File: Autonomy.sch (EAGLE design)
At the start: 5 parts, among them J1 APP_2POS_CONFIG12V_HORIZ, K1 PIN20X2, U1 OKI-78SR-5/1.5-W36HC

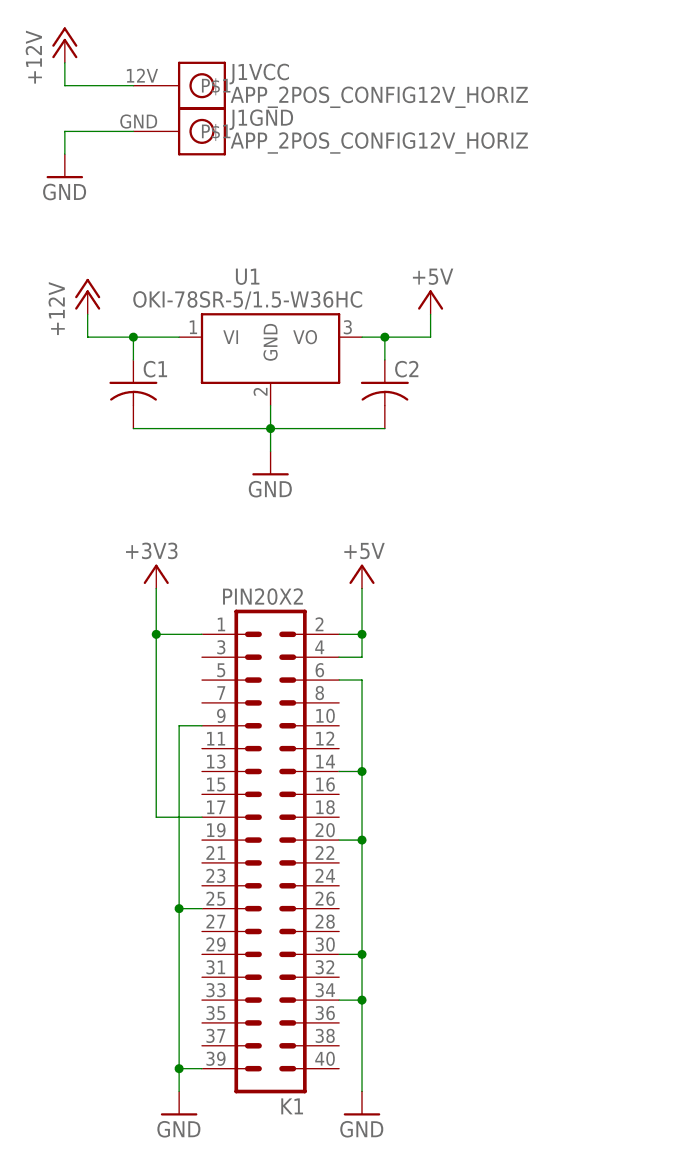
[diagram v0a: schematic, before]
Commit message: Cleaned up board, added power LED and board label
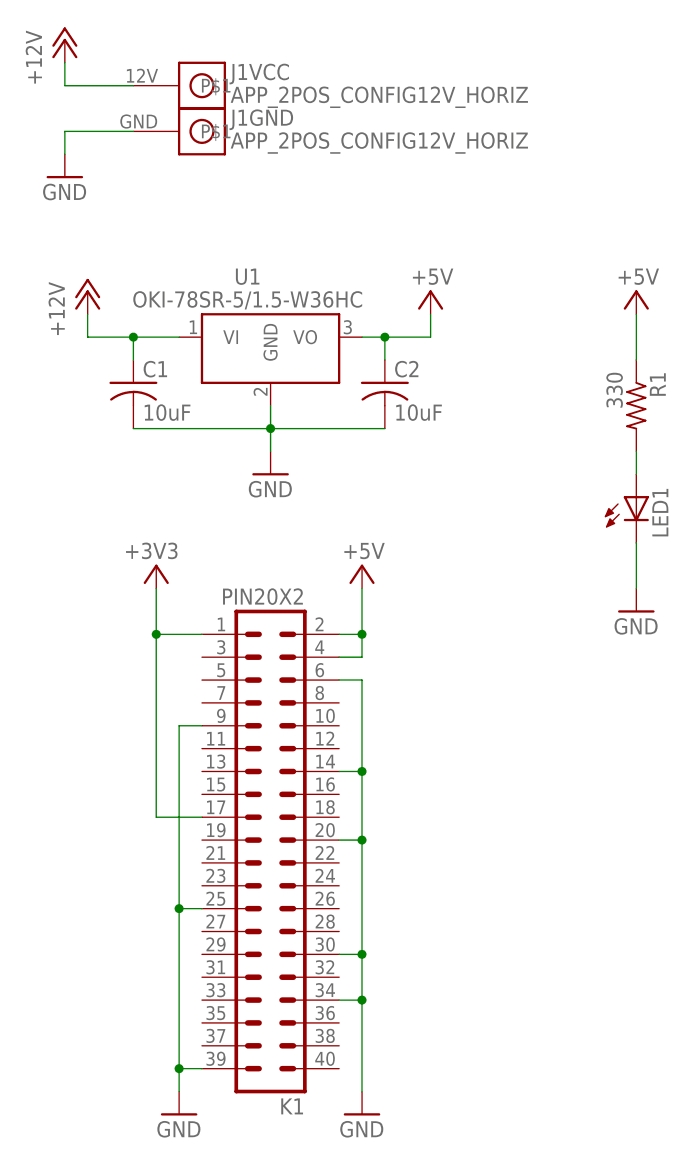
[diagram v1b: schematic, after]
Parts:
- added LED1: (no value), led:LEDCHIPLED_1206
- added R1: 330, rcl:R-US_R1206
- C1, C2: value (none) -> 10uF
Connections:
- new net N$1: LED1.A, R1.2
- net +5V: now also R1.1
- net GND: now also LED1.C
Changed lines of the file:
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@@
 <?xml version="1.0" encoding="utf-8"?>
 <!DOCTYPE eagle SYSTEM "eagle.dtd">
-<eagle version="7.4.0">
+<eagle version="7.5.0">
 <drawing>
 <settings>
@@
 <part name="GND2" library="supply1" deviceset="GND" device=""/>
 <part name="P+4" library="supply1" deviceset="+5V" device=""/>
-<part name="C1" library="rcl" deviceset="C-US" device="C1206"/>
-<part name="C2" library="rcl" deviceset="C-US" device="C1206"/>
+<part name="C1" library="rcl" deviceset="C-US" device="C1206" value="10uF"/>
+<part name="C2" library="rcl" deviceset="C-US" device="C1206" value="10uF"/>
+<part name="P+5" library="supply1" deviceset="+5V" device=""/>
+<part name="LED1" library="led" deviceset="LED" device="CHIPLED_1206"/>
+<part name="R1" library="rcl" deviceset="R-US_" device="R1206" value="330"/>
+<part name="GND4" library="supply1" deviceset="GND" device=""/>
 </parts>
 <sheets>
@@
 <instance part="C1" gate="G$1" x="30.48" y="22.86"/>
 <instance part="C2" gate="G$1" x="58.42" y="22.86"/>
+<instance part="P+5" gate="1" x="86.36" y="33.02" smashed="yes">
+<attribute name="VALUE" x="88.9" y="35.56" size="1.778" layer="96" rot="R180"/>
+</instance>
+<instance part="LED1" gate="G$1" x="86.36" y="10.16"/>
+<instance part="R1" gate="G$1" x="86.36" y="20.32" rot="R270"/>
+<instance part="GND4" gate="1" x="86.36" y="-2.54"/>
 </instances>
 <busses>
@@
 <wire x1="22.86" y1="50.8" x2="30.48" y2="50.8" width="0.1524" layer="91"/>
 </segment>
+<segment>
+<pinref part="GND4" gate="1" pin="GND"/>
+<pinref part="LED1" gate="G$1" pin="C"/>
+<wire x1="86.36" y1="0" x2="86.36" y2="5.08" width="0.1524" layer="91"/>
+</segment>
 </net>
 <net name="+3V3" class="0">
@@
 <junction x="58.42" y="27.94"/>
 </segment>
+<segment>
+<pinref part="P+5" gate="1" pin="+5V"/>
+<pinref part="R1" gate="G$1" pin="1"/>
+<wire x1="86.36" y1="25.4" x2="86.36" y2="30.48" width="0.1524" layer="91"/>
+</segment>
 </net>
 <net name="+12V" class="0">
@@
 </segment>
 </net>
+<net name="N$1" class="0">
+<segment>
+<pinref part="LED1" gate="G$1" pin="A"/>
+<pinref part="R1" gate="G$1" pin="2"/>
+<wire x1="86.36" y1="12.7" x2="86.36" y2="15.24" width="0.1524" layer="91"/>
+</segment>
+</net>

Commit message: Removed unnecessary 3v3 net and swapped header with eagle standard part
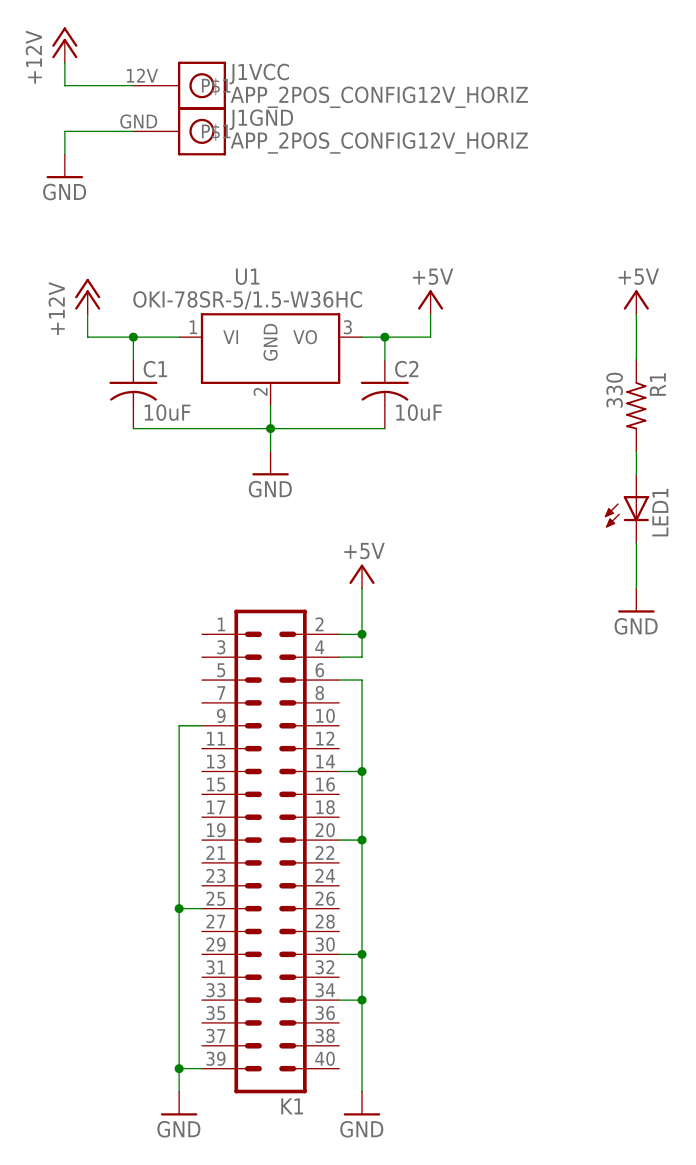
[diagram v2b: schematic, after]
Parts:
- K1: value PIN20X2 -> (none); device FLYFISH:PIN20X2 -> con-lstb:MA20-2
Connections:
- removed net +3V3: K1.1, K1.17
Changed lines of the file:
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@@
 </classes>
 <parts>
-<part name="K1" library="FLYFISH" deviceset="PIN20X2" device=""/>
+<part name="K1" library="con-lstb" deviceset="MA20-2" device=""/>
 <part name="GND10" library="supply1" deviceset="GND" device=""/>
-<part name="+3V1" library="supply1" deviceset="+3V3" device=""/>
 <part name="GND3" library="supply1" deviceset="GND" device=""/>
 <part name="P+1" library="supply1" deviceset="+5V" device=""/>
@@
 </plain>
 <instances>
-<instance part="K1" gate="G$1" x="45.72" y="-27.94" rot="R180"/>
+<instance part="K1" gate="G$1" x="45.72" y="-30.48" rot="R180"/>
 <instance part="GND10" gate="1" x="55.88" y="-58.42"/>
-<instance part="+3V1" gate="G$1" x="33.02" y="2.54" smashed="yes">
-<attribute name="VALUE" x="35.56" y="5.08" size="1.778" layer="96" rot="R180"/>
-</instance>
 <instance part="GND3" gate="1" x="35.56" y="-58.42"/>
 <instance part="P+1" gate="1" x="55.88" y="2.54" smashed="yes">
@@
 </segment>
 </net>
-<net name="+3V3" class="0">
-<segment>
-<pinref part="K1" gate="G$1" pin="1"/>
-<pinref part="+3V1" gate="G$1" pin="+3V3"/>
-<wire x1="38.1" y1="-5.08" x2="33.02" y2="-5.08" width="0.1524" layer="91"/>
-<wire x1="33.02" y1="-5.08" x2="33.02" y2="0" width="0.1524" layer="91"/>
-<pinref part="K1" gate="G$1" pin="17"/>
-<wire x1="38.1" y1="-25.4" x2="33.02" y2="-25.4" width="0.1524" layer="91"/>
-<wire x1="33.02" y1="-25.4" x2="33.02" y2="-5.08" width="0.1524" layer="91"/>
-<junction x="33.02" y="-5.08"/>
-</segment>
-</net>
